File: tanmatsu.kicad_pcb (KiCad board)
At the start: 4 copper layers, 114.9 x 129.9 mm, 362 parts, among them CN1 DF37NB-24DS-0.4V(51), J1 USB host, J10 External Add-On (SAO / PMOD), J11 Battery, J12 GND, J13 Sensor, J14 3.3v, J15 SDA, J16 SCL, J2 Micro_SD_Card, J3 USB device, J4 Headphone, J5 Speaker, J6 CAMERA, J7 SAO, J8 Expansion I3C, J9 Internal Add-On, Q1 AP2302B, Q2 AP2302B, Q3 AP2302B, Q4 AP2302B, SW1 Boot, SW2 User, SW3 Power, U1 USBLC6-2P6, U10 W25Q128JVS, U11 CH32V203C8T6, U12 74LVC2G02HD4-7, U13 Keyboard, U14 LR8341A-M25, U15 BQ25895RTW, U16 TPS63020DSJR, U17 AP3032KTR, U18 AP3032KTR, U19 SY6280AAC, U2 CH334R, U20 ESP32-C6-WROOM-1, U21 E22-900M22S, U22 74LVC1GU04, U23 IR968-8P(X1-X4)XBY, U24 ES8156, U25 FM8002A, U26 74LVC1G17GW,125, U27 SK6805, U28 SK6805, U29 SK6805, U3 TPD4E05U06DQAR, U30 SK6805, U31 SK6805, U32 SK6805, U33 BMI270, U4 USBLC6-2P6, U5 ESD, U6 ESD, U7 TLV62569DBV, U8 ESP32-P4, U9 TXB0104RGY, Y1 12MHz, Y2 40MHz, Y3 32.768KHz

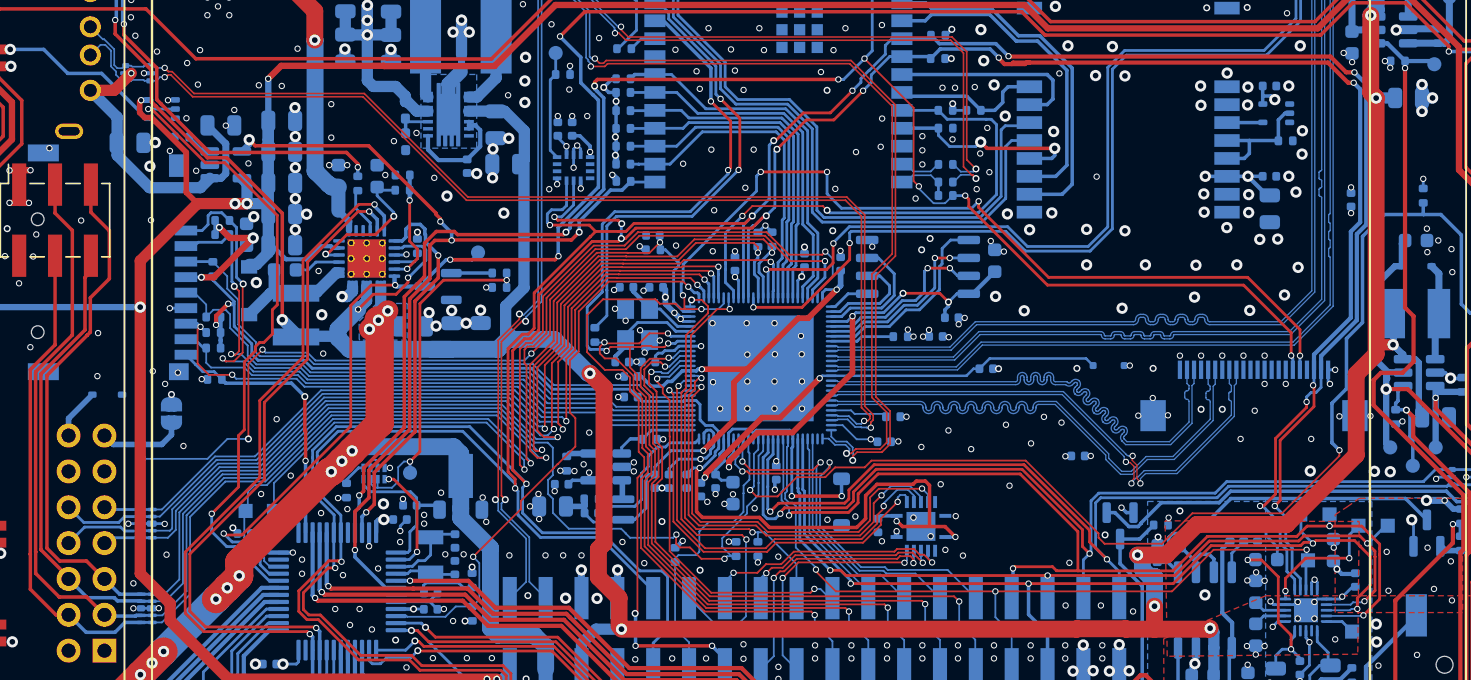
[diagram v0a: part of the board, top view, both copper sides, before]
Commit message: Rev 6 (#17)
* Change SD card power circuit, change LCSC part for L1, change camera connector

* Enable IR LED for assembly, hide unwanted fields of P4 on schematic
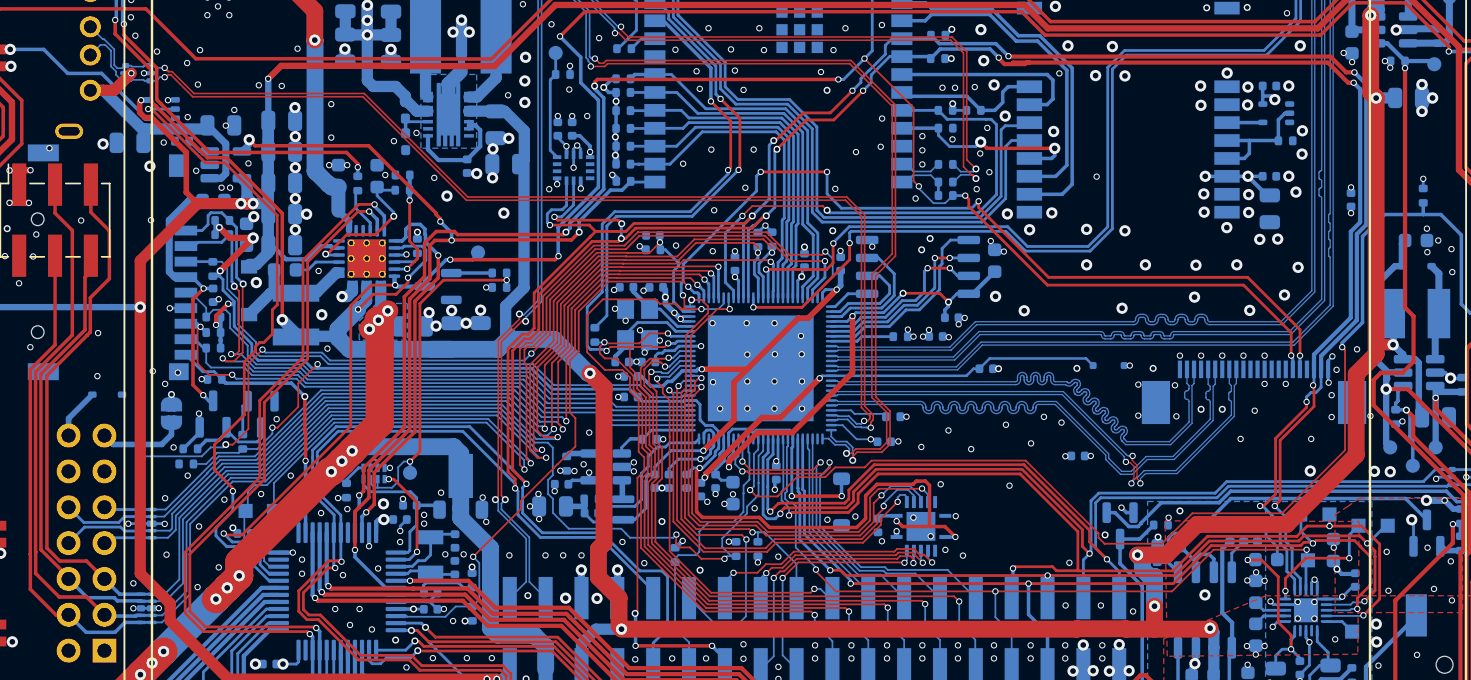
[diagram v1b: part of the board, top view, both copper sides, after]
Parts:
- added C87: 1u, Capacitor_SMD:C_0603_1608Metric, B.Cu at (-38.8, -36.9)
- added C88: 100n, Capacitor_SMD:C_0402_1005Metric, B.Cu at (-38.8, -30.2)
- added Q5: AO3401A, Package_TO_SOT_SMD:SOT-23, B.Cu at (-38.8, -21.8)
- added Q6: AP2302B, Package_TO_SOT_SMD:SOT-23, B.Cu at (-35.4, -21.7)
- added R83: 100k, Resistor_SMD:R_0402_1005Metric, B.Cu at (-40.4, -19.3)
- added R84: 10k, Resistor_SMD:R_0402_1005Metric, B.Cu at (-36.7, -19.8)
- added R85: 1M, Resistor_SMD:R_0402_1005Metric, B.Cu at (-40.7, -18.2)
- J6: footprint Connector_FFC-FPC:Hirose_FH12-22S-0.5SH_1x22-1MP_P0.50mm_Horizontal -> library:FPC-SMD_XUNPU_FPC-0.5FX-22PWBH20
- moved J6 0.70 mm to (35.0, -23.8)
- moved R53 0.29 mm to (-41.0, -41.1)
- turned C63 to 180 degrees
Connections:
- J2 pad 4: VSDCARD -> Net-(J2-VDD)
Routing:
- net Net-(J2-VDD): track 0.00 -> 19.2 mm, vias 0 -> 2
- net VSDCARD: track 96.0 -> 106.8 mm, vias 8 -> 10
- net /Application processor/SD_PWR_ENA: track 0.00 -> 6.78 mm
- net +3.3V: track 131.1 -> 134.5 mm, vias 75 -> 76
- net VOTG_OUT: track 22.3 -> 19.6 mm
- net Net-(Q6-G): track 0.00 -> 2.51 mm
- net /Coprocessor/LED_DATA: track 44.9 -> 45.7 mm
- net GND: track 82.5 -> 83.0 mm, vias 536 -> 549
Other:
- board text added: "QWIIC"
- board text added: "Rev. 6"
- board text removed: "I3C"
